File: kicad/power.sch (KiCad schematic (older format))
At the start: 17 parts, among them J4 UE27AC54100, Q1 PN2222A, U3 P-FET, U4 LM3671MF-3.3

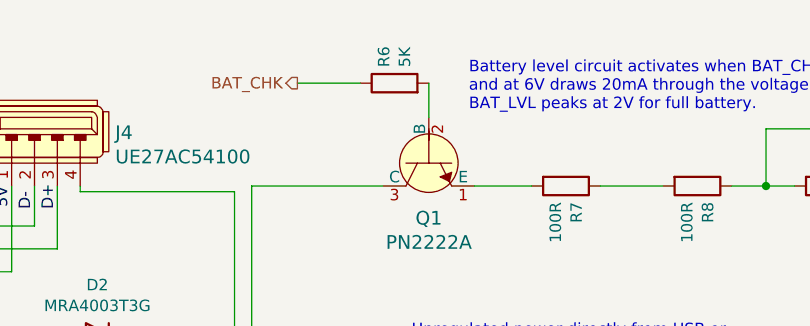
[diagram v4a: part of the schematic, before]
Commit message: Fix register footprints and add batt indicator
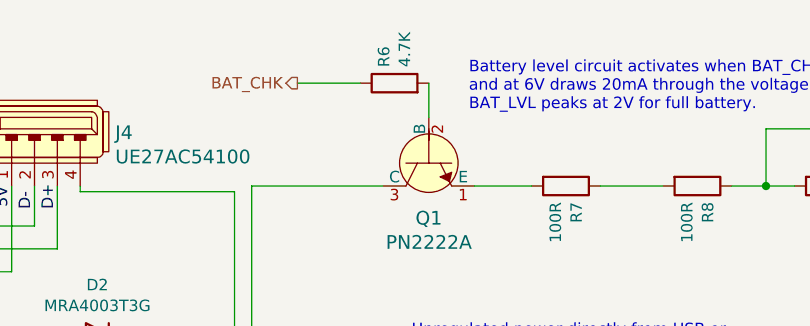
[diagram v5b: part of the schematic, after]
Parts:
- Q1: footprint digikey-footprints:TO-92-3 -> Package_TO_SOT_THT:TO-92_Inline_W4.0mm_Horizontal_FlatSideDown
- R6: value 5K -> 4.7K
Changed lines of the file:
@@
 F 0 "Q1" V 5591 2100 60  0000 C CNN
 F 1 "PN2222A" V 5697 2100 60  0000 C CNN
-F 2 "digikey-footprints:TO-92-3" H 5550 2300 60  0001 L CNN
+F 2 "Package_TO_SOT_THT:TO-92_Inline_W4.0mm_Horizontal_FlatSideDown" H 5550 2300 60  0001 L CNN
 F 3 "https://my.centralsemi.com/get_document.php?cmp=1&mergetype=pd&mergepath=pd&pdf_id=PN2221-2222A.PDF" H 5550 2400 60  0001 L CNN
 F 4 "PN2222ACS-ND" H 5550 2500 60  0001 L CNN "Digi-Key_PN"
@@
 P 5200 1750
 F 0 "R6" H 5270 1796 50  0000 L CNN
-F 1 "5K" H 5270 1705 50  0000 L CNN
+F 1 "4.7K" H 5270 1705 50  0000 L CNN
 F 2 "Resistor_SMD:R_0805_2012Metric_Pad1.15x1.40mm_HandSolder" V 5130 1750 50  0001 C CNN
 F 3 "~" H 5200 1750 50  0001 C CNN

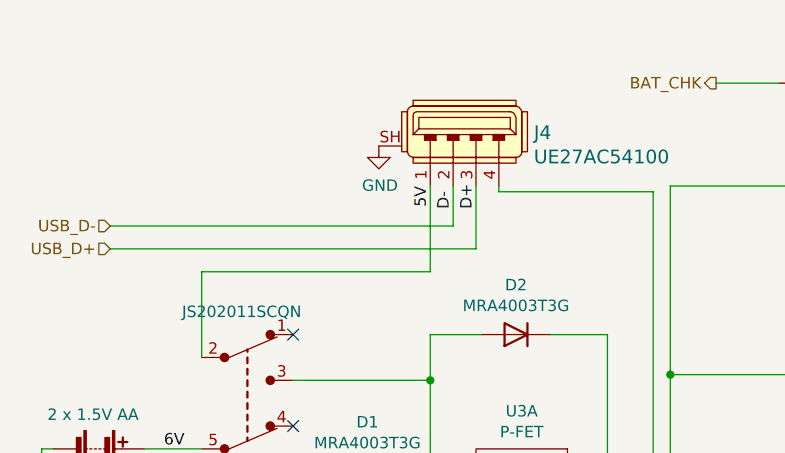
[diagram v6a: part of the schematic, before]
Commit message: Disconnect USB shield from ground plane
Also Fixed obscured refdes indicators.
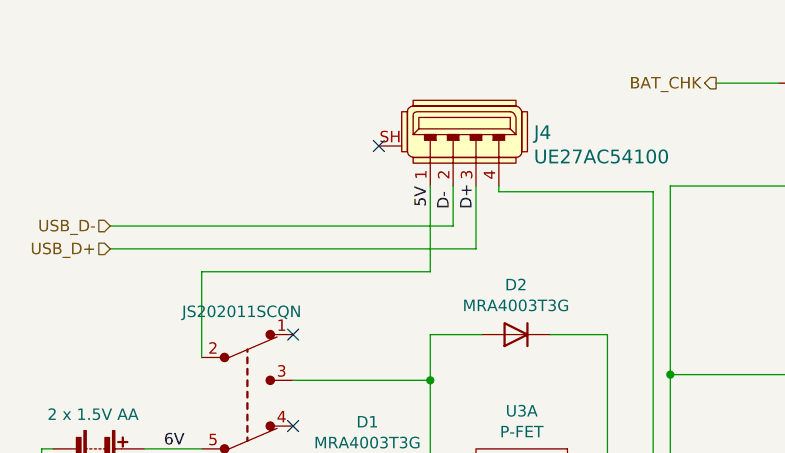
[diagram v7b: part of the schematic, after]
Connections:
- net GND: no longer J4.SH
- no-connect marks 4 -> 5
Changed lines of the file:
@@
 Wire Wire Line
 	5075 3450 4925 3450
-$Comp
-L power:GND #PWR014
-U 1 1 5F8DC955
-P 3300 2025
-F 0 "#PWR014" H 3300 1775 50  0001 C CNN
-F 1 "GND" H 3305 1852 50  0000 C CNN
-F 2 "" H 3300 2025 50  0001 C CNN
-F 3 "" H 3300 2025 50  0001 C CNN
-	1    3300 2025
-	1    0    0    -1
-$EndComp
 Wire Wire Line
 	4575 3450 4575 3025
@@
 NoConn ~ 2925 2850
 NoConn ~ 2925 3250
+NoConn ~ 3300 2025
 $EndSCHEMATC
